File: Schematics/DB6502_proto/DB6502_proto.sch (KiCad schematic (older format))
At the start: 20 parts, among them U1 74HC21, U2 74AC74, U3 74AC04, U4 65C02S, U5 62256, U6 22V10C, U7 62256, U8 74AC138, U9 28C256

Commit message: Working on the second PCB
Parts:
- added C7: 22pF, Capacitor_THT:C_Disc_D5.0mm_W2.5mm_P2.50mm, symbol Device:C_Small
- added JP1: PLD CLK Selector, Connector_PinSocket_2.54mm:PinSocket_1x03_P2.54mm_Vertical, symbol Jumper:Jumper_3_Open
- added JP2: PLD ~WR, Connector_PinHeader_2.54mm:PinHeader_1x02_P2.54mm_Vertical, symbol Jumper:Jumper_2_Open
- added JP3: PLD ~RD, Connector_PinHeader_2.54mm:PinHeader_1x02_P2.54mm_Vertical, symbol Jumper:Jumper_2_Open
- added JP4: PLD RDY, Connector_PinHeader_2.54mm:PinHeader_1x02_P2.54mm_Vertical, symbol Jumper:Jumper_2_Open
- added JP5: PLD DBG_WAIT, Connector_PinHeader_2.54mm:PinHeader_1x02_P2.54mm_Vertical, symbol Jumper:Jumper_2_Open
- added JP6: PLD WS_DISABLE, Connector_PinHeader_2.54mm:PinHeader_1x02_P2.54mm_Vertical, symbol Jumper:Jumper_2_Open
- added JP7: PLD RDY_M1F, Connector_PinHeader_2.54mm:PinHeader_1x02_P2.54mm_Vertical, symbol Jumper:Jumper_2_Open
- added JP8: PLD RDY_M2F, Connector_PinHeader_2.54mm:PinHeader_1x02_P2.54mm_Vertical, symbol Jumper:Jumper_2_Open
- added R4: 4K7, Resistor_THT:R_Axial_DIN0207_L6.3mm_D2.5mm_P10.16mm_Horizontal, symbol Device:R
- added TP1, TP2: TestPoint, TestPoint:TestPoint_Keystone_5005-5009_Compact, symbol Connector:TestPoint
- added unit 6 of U8
- C1: renamed from C4; footprint Capacitor_THT:C_Disc_D5.0mm_W2.5mm_P2.50mm -> Capacitor_SMD:C_0805_2012Metric_Pad1.15x1.40mm_HandSolder
- C2: renamed from C6; footprint Capacitor_THT:C_Disc_D5.0mm_W2.5mm_P2.50mm -> Capacitor_SMD:C_0805_2012Metric_Pad1.15x1.40mm_HandSolder
- C3: renamed from C8; footprint Capacitor_THT:C_Disc_D5.0mm_W2.5mm_P2.50mm -> Capacitor_SMD:C_0805_2012Metric_Pad1.15x1.40mm_HandSolder
- C4: renamed from C1; footprint Capacitor_THT:C_Disc_D5.0mm_W2.5mm_P2.50mm -> Capacitor_SMD:C_0805_2012Metric_Pad1.15x1.40mm_HandSolder
- C5: renamed from C7; footprint Capacitor_THT:C_Disc_D5.0mm_W2.5mm_P2.50mm -> Capacitor_SMD:C_0805_2012Metric_Pad1.15x1.40mm_HandSolder
- C6: renamed from C5; footprint Capacitor_THT:C_Disc_D5.0mm_W2.5mm_P2.50mm -> Capacitor_SMD:C_0805_2012Metric_Pad1.15x1.40mm_HandSolder
- C8: renamed from C2; footprint Capacitor_THT:C_Disc_D5.0mm_W2.5mm_P2.50mm -> Capacitor_SMD:C_0805_2012Metric_Pad1.15x1.40mm_HandSolder
- C9: renamed from C3; footprint Capacitor_THT:C_Disc_D5.0mm_W2.5mm_P2.50mm -> Capacitor_SMD:C_0805_2012Metric_Pad1.15x1.40mm_HandSolder
- R1: value 4K7 -> 470
- U2: renamed from U7; value 62256 -> 71256; footprint Package_DIP:DIP-28_W15.24mm_Socket -> Package_DIP:DIP-28_W7.62mm_Socket
- U3: renamed from U9; value 28C256 -> 71256; footprint Package_DIP:DIP-28_W15.24mm_Socket -> Package_DIP:DIP-28_W7.62mm_Socket
- U9: renamed from U1; footprint Package_DIP:DIP-12_W7.62mm_Socket -> Package_DIP:DIP-14_W7.62mm_Socket
- renumbered U5 to U1, U2 to U5, U8 to U6, U6 to U7, U3 to U8
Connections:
- net +5V: now also R4.1; no longer R1.1
- net 6502_CLK: now also U8.8, JP1.1 (A); no longer U7.1 (CLK/IN1), U8.9
- net 6502_RDY: now also C7.2, JP4.2 (B), TP1.1; no longer U4.2 (RDY), U7.17 (IO16)
- net DBG_WAIT: now also JP5.2 (B); no longer U7.16 (IO15)
- net RDY_M1F: now also JP8.2 (B); no longer U7.13 (IN12)
- net RDY_M2F: now also JP7.2 (B); no longer U7.14 (IO13)
- net WS_DISABLE: now also JP6.2 (B); no longer U7.15 (IO14)
- net ~RD: now also JP3.2 (B); no longer U7.22 (IO21)
- net ~VIA2_IRQ: now also R4.2
- net ~WR: now also JP2.2 (B); no longer U7.23 (IO22)
- net ~6502_CLK: now reaches U5.11 (C), U5.3 (C)
- net ~6502_CLK: now also U8.9, JP1.3 (B), U8.12; no longer U8.8
- new net 6502_CLK_IN: U8.13
- new net 6502_RDY_IN: C7.1, R1.1, TP2.1, U4.2 (RDY)
- new net IN12: JP8.1 (A), U7.13 (IN12)
- new net IO13: JP7.1 (A), U7.14 (IO13)
- new net IO14: JP6.1 (A), U7.15 (IO14)
- new net IO15: JP5.1 (A), U7.16 (IO15)
- new net IO16: JP4.1 (A), U7.17 (IO16)
- new net PLD_CLK: JP1.2 (C), U7.1 (CLK/IN1)
- new net ~PLD_RD: JP3.1 (A), U7.22 (IO21)
- new net ~PLD_WR: JP2.1 (A), U7.23 (IO22)
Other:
- moved on the sheet: C4, R2, R3, U5A, U5B, U8D

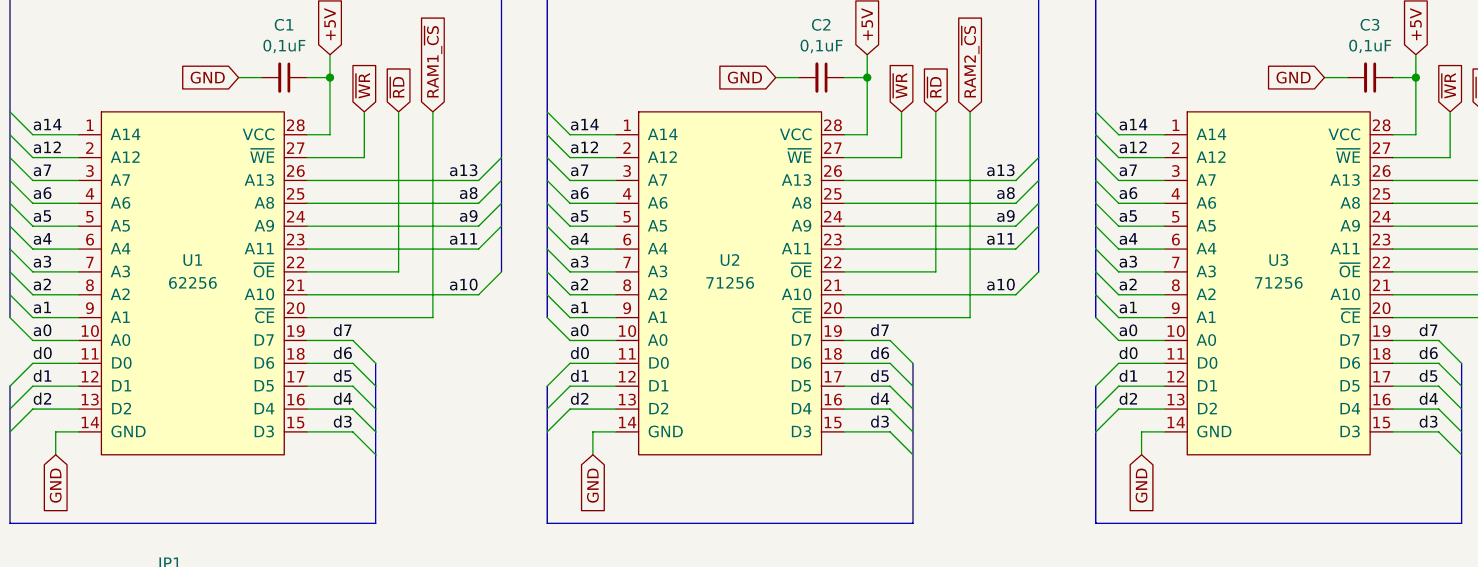
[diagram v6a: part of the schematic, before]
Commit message: Updated RAM/ROM footprints
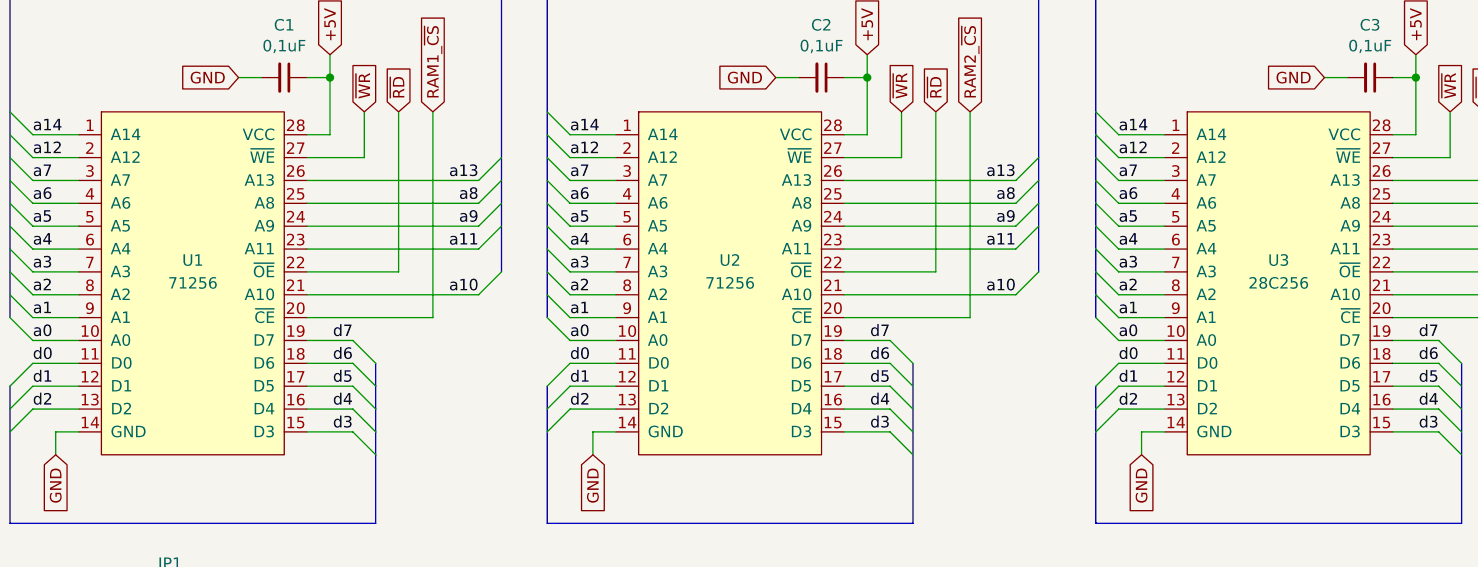
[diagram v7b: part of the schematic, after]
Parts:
- U1: value 62256 -> 71256; footprint Package_DIP:DIP-28_W15.24mm_Socket -> Package_DIP:DIP-28_W7.62mm_Socket
- U3: value 71256 -> 28C256; footprint Package_DIP:DIP-28_W7.62mm_Socket -> Package_DIP:DIP-28_W15.24mm_Socket
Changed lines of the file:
@@
 AR Path="/5FE5FF2A/5FD9D8A7" Ref="U?"  Part="1"
 F 0 "U1" H 4850 2000 50  0000 C CNN
-F 1 "62256" H 4850 1900 50  0000 C CNN
-F 2 "Package_DIP:DIP-28_W15.24mm_Socket" H 4800 2700 50  0001 C CNN
+F 1 "71256" H 4850 1900 50  0000 C CNN
+F 2 "Package_DIP:DIP-28_W7.62mm_Socket" H 4800 2700 50  0001 C CNN
 F 3 "" H 4850 1900 50  0001 C CNN
 	1    4850 1900
@@
 AR Path="/5FE5FF2A/5FD9D8AD" Ref="U?"  Part="1"
 F 0 "U3" H 9600 2000 50  0000 C CNN
-F 1 "71256" H 9600 1900 50  0000 C CNN
-F 2 "Package_DIP:DIP-28_W7.62mm_Socket" H 9550 2700 50  0001 C CNN
+F 1 "28C256" H 9600 1900 50  0000 C CNN
+F 2 "Package_DIP:DIP-28_W15.24mm_Socket" H 9550 2700 50  0001 C CNN
 F 3 "" H 9600 1900 50  0001 C CNN
 	1    9600 1900

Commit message: Working on a PCB - first traces routed
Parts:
- U5, U8, U9: footprint Package_DIP:DIP-14_W7.62mm_Socket -> Package_SO:SOIC-14_3.9x8.7mm_P1.27mm
- U6: footprint Package_DIP:DIP-16_W7.62mm_Socket -> Package_SO:SOIC-16_3.9x9.9mm_P1.27mm
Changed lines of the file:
@@
 F 0 "U6" H 9250 4350 50  0000 C CNN
 F 1 "74AC138" H 9150 4250 50  0000 C CNN
-F 2 "Package_DIP:DIP-16_W7.62mm_Socket" H 9250 4350 50  0001 C CNN
+F 2 "Package_SO:SOIC-16_3.9x9.9mm_P1.27mm" H 9250 4350 50  0001 C CNN
 F 3 "http://www.ti.com/lit/gpn/sn74LS138" H 9250 4350 50  0001 C CNN
 	1    9250 4350
@@
 F 0 "U9" H 5950 7675 50  0000 C CNN
 F 1 "74HC21" H 5950 7584 50  0000 C CNN
-F 2 "Package_DIP:DIP-14_W7.62mm_Socket" H 5950 7300 50  0001 C CNN
+F 2 "Package_SO:SOIC-14_3.9x8.7mm_P1.27mm" H 5950 7300 50  0001 C CNN
 F 3 "http://www.ti.com/lit/gpn/sn74LS21" H 5950 7300 50  0001 C CNN
 	1    5950 7300
@@
 F 0 "U9" H 3250 7675 50  0000 C CNN
 F 1 "74HC21" H 3250 7584 50  0000 C CNN
-F 2 "Package_DIP:DIP-14_W7.62mm_Socket" H 3250 7300 50  0001 C CNN
+F 2 "Package_SO:SOIC-14_3.9x8.7mm_P1.27mm" H 3250 7300 50  0001 C CNN
 F 3 "http://www.ti.com/lit/gpn/sn74LS21" H 3250 7300 50  0001 C CNN
 	2    3250 7300
@@
 F 0 "U9" H 1000 7050 50  0000 C CNN
 F 1 "74HC21" H 1000 6950 50  0000 C CNN
-F 2 "Package_DIP:DIP-14_W7.62mm_Socket" H 1000 7000 50  0001 C CNN
+F 2 "Package_SO:SOIC-14_3.9x8.7mm_P1.27mm" H 1000 7000 50  0001 C CNN
 F 3 "http://www.ti.com/lit/gpn/sn74LS21" H 1000 7000 50  0001 C CNN
 	3    1000 7000
@@
 F 0 "U5" H 1850 7050 50  0000 C CNN
 F 1 "74AC74" H 1850 6950 50  0000 C CNN
-F 2 "Package_DIP:DIP-14_W7.62mm_Socket" H 1850 7000 50  0001 C CNN
+F 2 "Package_SO:SOIC-14_3.9x8.7mm_P1.27mm" H 1850 7000 50  0001 C CNN
 F 3 "74xx/74hc_hct74.pdf" H 1850 7000 50  0001 C CNN
 	3    1850 7000
@@
 F 0 "U5" H 2650 4600 50  0000 C CNN
 F 1 "74AC74" H 2650 4500 50  0000 C CNN
-F 2 "Package_DIP:DIP-14_W7.62mm_Socket" H 2950 4200 50  0001 C CNN
+F 2 "Package_SO:SOIC-14_3.9x8.7mm_P1.27mm" H 2950 4200 50  0001 C CNN
 F 3 "74xx/74hc_hct74.pdf" H 2950 4200 50  0001 C CNN
 	2    2950 4200
@@
 F 0 "U5" H 1550 4600 50  0000 C CNN
 F 1 "74AC74" H 1550 4500 50  0000 C CNN
-F 2 "Package_DIP:DIP-14_W7.62mm_Socket" H 1850 4200 50  0001 C CNN
+F 2 "Package_SO:SOIC-14_3.9x8.7mm_P1.27mm" H 1850 4200 50  0001 C CNN
 F 3 "74xx/74hc_hct74.pdf" H 1850 4200 50  0001 C CNN
 	1    1850 4200
@@
 F 0 "U8" H 2650 5517 50  0000 C CNN
 F 1 "74AC04" H 2650 5426 50  0000 C CNN
-F 2 "Package_DIP:DIP-14_W7.62mm_Socket" H 2650 5200 50  0001 C CNN
+F 2 "Package_SO:SOIC-14_3.9x8.7mm_P1.27mm" H 2650 5200 50  0001 C CNN
 F 3 "https://www.ti.com/lit/ds/symlink/sn74ac04.pdf" H 2650 5200 50  0001 C CNN
 	4    2650 5200
@@
 F 0 "U8" H 1850 5517 50  0000 C CNN
 F 1 "74AC04" H 1850 5426 50  0000 C CNN
-F 2 "Package_DIP:DIP-14_W7.62mm_Socket" H 1850 5200 50  0001 C CNN
+F 2 "Package_SO:SOIC-14_3.9x8.7mm_P1.27mm" H 1850 5200 50  0001 C CNN
 F 3 "https://www.ti.com/lit/ds/symlink/sn74ac04.pdf" H 1850 5200 50  0001 C CNN
 	6    1850 5200
